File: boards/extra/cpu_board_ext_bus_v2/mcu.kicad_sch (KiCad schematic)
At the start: 8 parts, among them U1 Z80CPPLC44, U2 GAL16V8, U3 74LS244, U4 74LS244, U5 74LS245, U6 74LS244

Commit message: Preparation for ordering with PCBWay.
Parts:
- R3: MPN (none) -> MF0207FTE52-4K7; Manufacturer (none) -> YAGEO; Package (none) -> Plugin
- RN5: MPN (none) -> A05-472JP; Manufacturer (none) -> FH (Guangdong Fenghua Advanced Tech); Package (none) -> SIP-5-2.54mm
- U1: MPN (none) -> DS1032-44SDKT1A; Manufacturer (none) -> CONNFLY Elec; Package (none) -> Plugin-44P
- U2, U3, U4, U5, U6: MPN (none) -> 1-2199298-6; Manufacturer (none) -> TE Connectivity; Package (none) -> DIP-20
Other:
- moved on the sheet: U5, U6

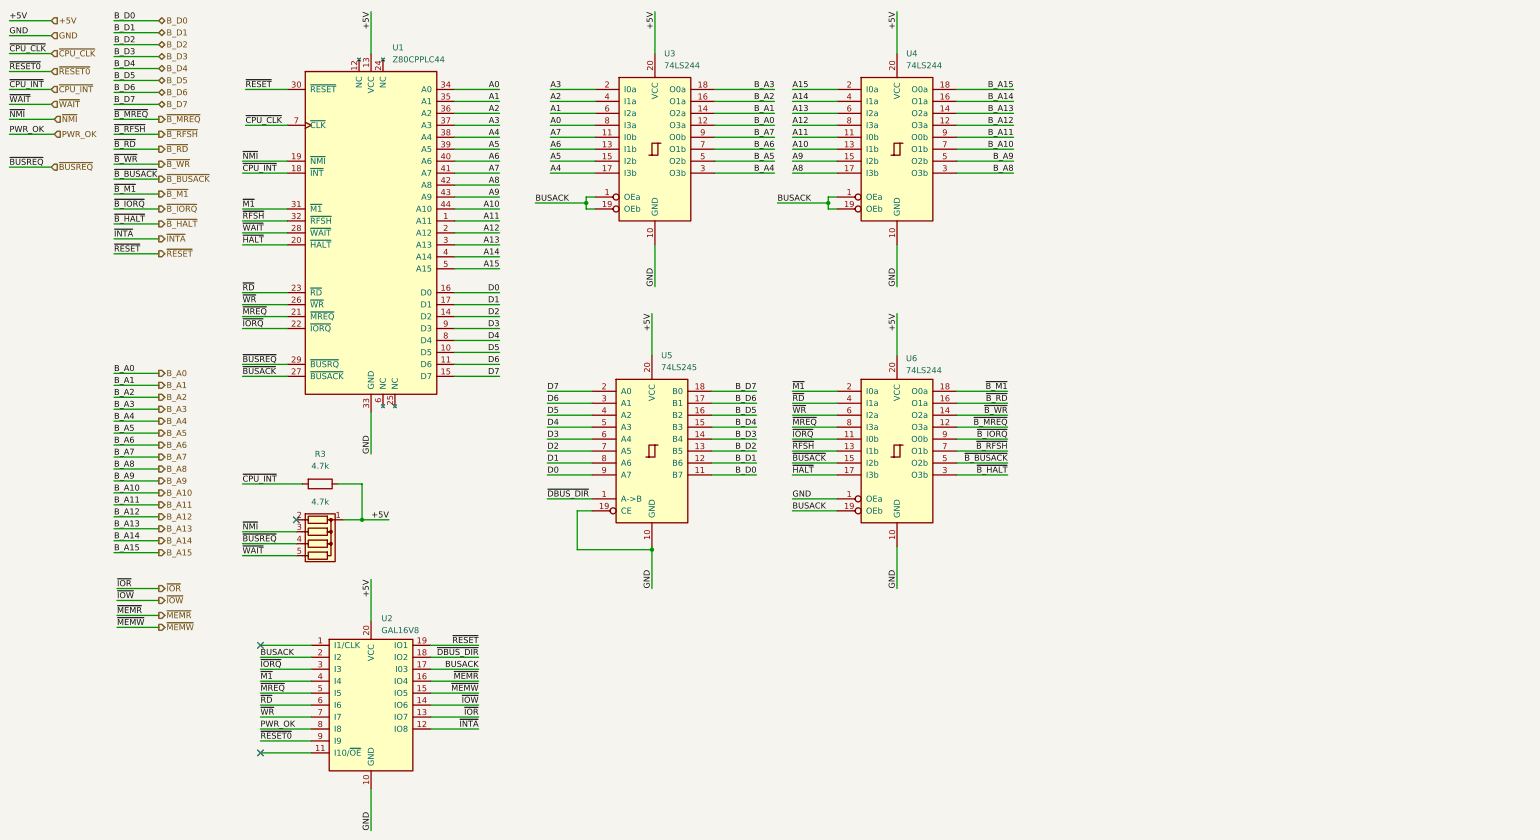
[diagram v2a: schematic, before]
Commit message: Upgraded board to KiCad 8 and imported design rules from the PCBWay website.
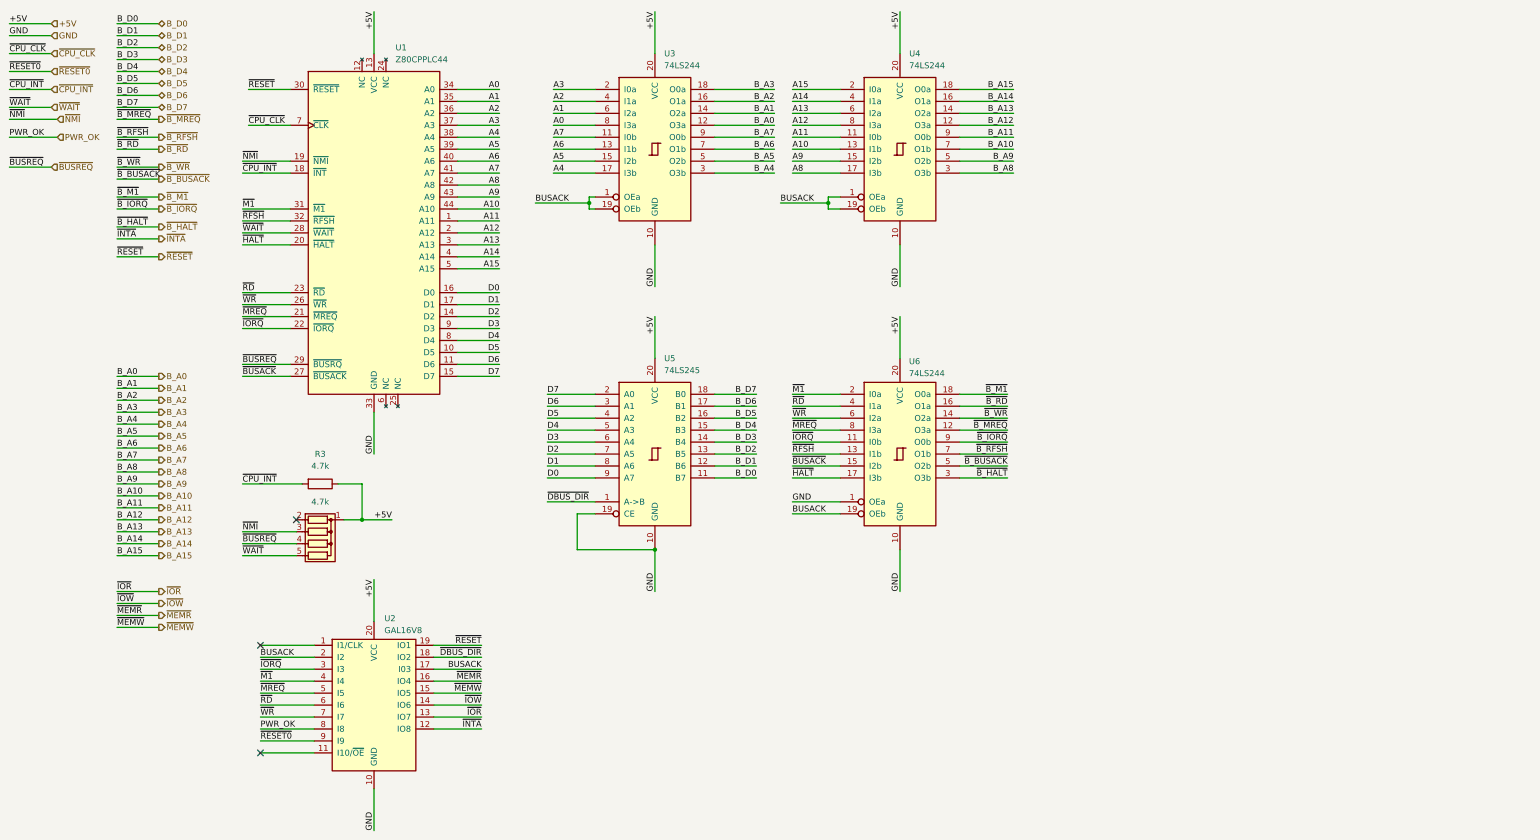
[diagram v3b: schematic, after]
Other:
- moved on the sheet: U1, U2, U4, U5, U6
